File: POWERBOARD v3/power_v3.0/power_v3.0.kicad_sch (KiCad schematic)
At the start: 0 parts

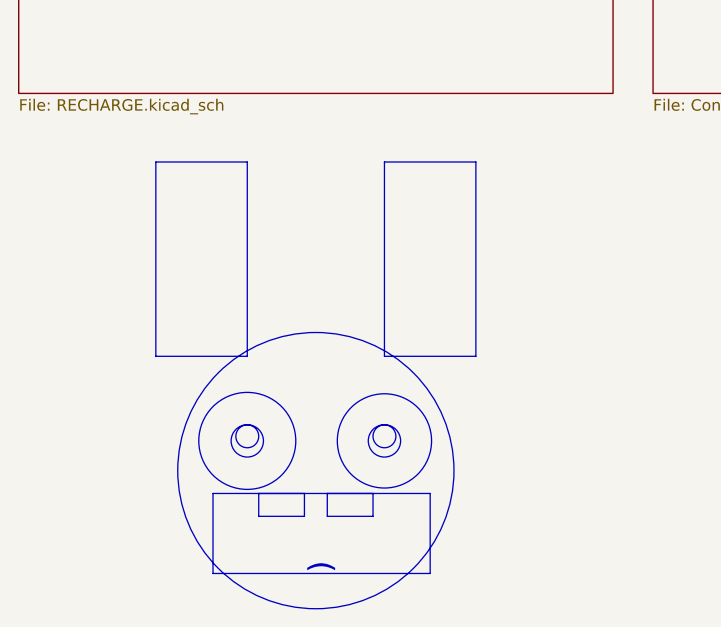
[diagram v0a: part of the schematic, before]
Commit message: added TVS diodes to charging circuit and (almost fully) routed 5.3 to 5V LDO
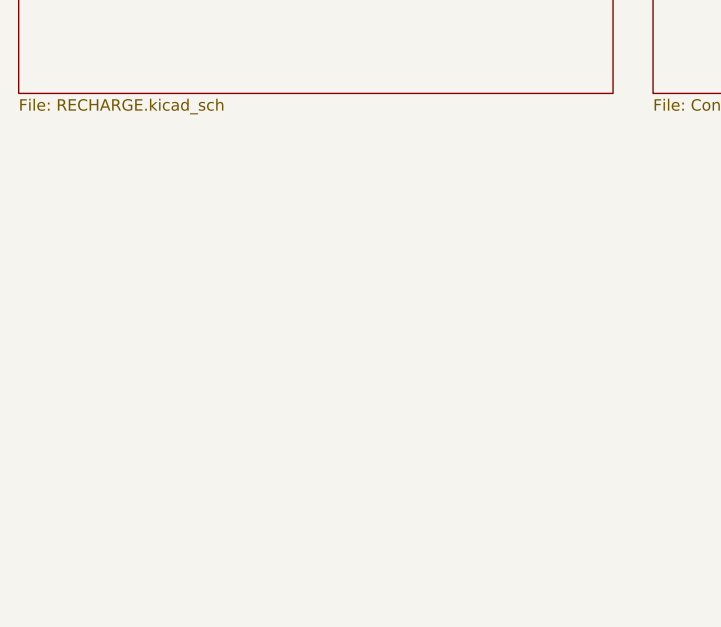
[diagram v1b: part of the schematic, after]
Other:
- note removed: ")"
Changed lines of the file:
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@@
 	(generator_version "10.0")
 	(paper "A4")
-	(rectangle
-		(start 60.96 167.64)
-		(end 85.09 176.53)
-		(stroke
-			(width 0)
-			(type default)
-		)
-		(fill
-			(type none)
-		)
-	)
-	(rectangle
-		(start 80.01 130.81)
-		(end 90.17 152.4)
-		(stroke
-			(width 0)
-			(type default)
-		)
-		(fill
-			(type none)
-		)
-	)
-	(rectangle
-		(start 66.04 167.64)
-		(end 71.12 170.18)
-		(stroke
-			(width 0)
-			(type default)
-		)
-		(fill
-			(type none)
-		)
-	)
-	(circle
-		(center 80.01 161.798)
-		(radius 1.7961)
-		(stroke
-			(width 0)
-			(type solid)
-		)
-		(fill
-			(type none)
-		)
-	)
-	(circle
-		(center 64.77 161.29)
-		(radius 1.27)
-		(stroke
-			(width 0)
-			(type solid)
-		)
-		(fill
-			(type none)
-		)
-	)
-	(circle
-		(center 64.77 161.798)
-		(radius 5.3882)
-		(stroke
-			(width 0)
-			(type default)
-		)
-		(fill
-			(type none)
-		)
-	)
-	(rectangle
-		(start 54.61 130.81)
-		(end 64.77 152.4)
-		(stroke
-			(width 0)
-			(type solid)
-		)
-		(fill
-			(type none)
-		)
-	)
-	(circle
-		(center 80.01 161.29)
-		(radius 1.27)
-		(stroke
-			(width 0)
-			(type default)
-		)
-		(fill
-			(type none)
-		)
-	)
-	(circle
-		(center 72.39 165.1)
-		(radius 15.3455)
-		(stroke
-			(width 0)
-			(type default)
-		)
-		(fill
-			(type none)
-		)
-	)
-	(circle
-		(center 64.77 161.798)
-		(radius 1.7961)
-		(stroke
-			(width 0)
-			(type default)
-		)
-		(fill
-			(type none)
-		)
-	)
-	(circle
-		(center 80.01 161.798)
-		(radius 5.2363)
-		(stroke
-			(width 0)
-			(type default)
-		)
-		(fill
-			(type none)
-		)
-	)
-	(rectangle
-		(start 73.66 167.64)
-		(end 78.74 170.18)
-		(stroke
-			(width 0)
-			(type default)
-		)
-		(fill
-			(type none)
-		)
-	)
-	(text ")\n"
-		(exclude_from_sim no)
-		(at 72.898 176.022 90)
-		(effects
-			(font
-				(size 2.54 2.54)
-			)
-		)
-	)
 	(sheet
 		(at 109.855 63.5)

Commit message: updated file names and added hierarchy schematic, problem with ERC bc of GND
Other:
- removed sheet Conversion 5.3V-5V (page 4)
- removed sheet Conversion battery-5.3V (page 2)
- added sheet Conversion 5.3-5V (5.3to5V.kicad_sch)
- added sheet Conversion battery-5.3V (Conversion battery-5.3V.kicad_sch)
- sheet Charging circuit ports: added SYS; removed none
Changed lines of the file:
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@@
 	(generator_version "10.0")
 	(paper "A4")
+	(text_box "FILE HIERARCHY"
+		(exclude_from_sim no)
+		(at 60.96 88.9 0)
+		(size 157.48 44.45)
+		(margins 0.9525 0.9525 0.9525 0.9525)
+		(stroke
+			(width 0)
+			(type solid)
+		)
+		(fill
+			(type none)
+		)
+		(effects
+			(font
+				(size 1.27 1.27)
+			)
+			(justify left top)
+		)
+	)
+	(wire
+		(pts
+			(xy 153.67 107.95) (xy 175.26 107.95)
+		)
+		(stroke
+			(width 0)
+			(type default)
+		)
+	)
+	(wire
+		(pts
+			(xy 102.87 107.95) (xy 124.46 107.95)
+		)
+		(stroke
+			(width 0)
+			(type default)
+		)
+	)
 	(sheet
-		(at 109.855 63.5)
-		(size 67.31 59.69)
+		(at 124.46 102.87)
+		(size 29.21 19.05)
 		(exclude_from_sim no)
 		(in_bom yes)
@@
 			(color 0 0 0 0)
 		)
-		(property "Sheetname" "Conversion battery-5.3V (page 2)"
-			(at 109.855 62.7884 0)
+		(property "Sheetname" "Conversion battery-5.3V"
+			(at 124.46 102.1584 0)
+			(hide yes)
 			(show_name no)
 			(do_not_autoplace no)
@@
 			)
 		)
-		(property "Sheetfile" "Converison battery-5V.kicad_sch"
-			(at 109.855 123.7746 0)
+		(property "Sheetfile" "Conversion battery-5.3V.kicad_sch"
+			(at 124.46 122.5046 0)
 			(show_name no)
 			(do_not_autoplace no)
@@
 				)
 				(justify left top)
+			)
+		)
+		(pin "SYS" input
+			(at 124.46 107.95 180)
+			(effects
+				(font
+					(size 1.27 1.27)
+				)
+				(justify left)
+			)
+		)
+		(pin "output_at_5.3" output
+			(at 153.67 107.95 0)
+			(effects
+				(font
+					(size 1.27 1.27)
+				)
+				(justify right)
 			)
 		)
@@
 	)
 	(sheet
-		(at 181.61 63.5)
-		(size 66.675 59.69)
+		(at 73.66 102.87)
+		(size 29.21 19.05)
 		(exclude_from_sim no)
 		(in_bom yes)
@@
 			(color 0 0 0 0)
 		)
-		(property "Sheetname" "Conversion 5.3V-5V (page 4)"
-			(at 181.61 62.7884 0)
+		(property "Sheetname" "Charging circuit"
+			(at 73.66 102.1584 0)
 			(show_name no)
 			(do_not_autoplace no)
@@
 			)
 		)
-		(property "Sheetfile" "5to3.3V.kicad_sch"
-			(at 181.61 123.7746 0)
+		(property "Sheetfile" "RECHARGE.kicad_sch"
+			(at 73.66 122.5046 0)
 			(show_name no)
 			(do_not_autoplace no)
@@
 				)
 				(justify left top)
+			)
+		)
+		(pin "SYS" output
+			(at 102.87 107.95 0)
+			(effects
+				(font
+					(size 1.27 1.27)
+				)
+				(justify right)
+			)
+		)
+		(instances
+			(project "power_v3.0"
+				(path "/432bcdcf-747a-4fa0-b87b-096f44260199"
+					(page "3")
+				)
+			)
+		)
+	)
+	(sheet
+		(at 175.26 102.87)
+		(size 29.21 19.05)
+		(exclude_from_sim no)
+		(in_bom yes)
+		(on_board yes)
+		(dnp no)
+		(fields_autoplaced yes)
+		(stroke
+			(width 0.1524)
+			(type solid)
+		)
+		(fill
+			(color 0 0 0 0)
+		)
+		(property "Sheetname" "Conversion 5.3-5V"
+			(at 175.26 102.1584 0)
+			(show_name no)
+			(do_not_autoplace no)
+			(effects
+				(font
+					(size 1.27 1.27)
+				)
+				(justify left bottom)
+			)
+		)
+		(property "Sheetfile" "5.3to5V.kicad_sch"
+			(at 175.26 122.5046 0)
+			(show_name no)
+			(do_not_autoplace no)
+			(effects
+				(font
+					(size 1.27 1.27)
+				)
+				(justify left top)
+			)
+		)
+		(pin "input_at_5.3" input
+			(at 175.26 107.95 180)
+			(effects
+				(font
+					(size 1.27 1.27)
+				)
+				(justify left)
 			)
 		)
@@
 				)
 			)
-		)
-	)
-	(sheet
-		(at 39.37 63.5)
-		(size 66.04 59.69)
-		(exclude_from_sim no)
-		(in_bom yes)
-		(on_board yes)
-		(dnp no)
-		(fields_autoplaced yes)
-		(stroke
-			(width 0.1524)
-			(type solid)
-		)
-		(fill
-			(color 0 0 0 0)
-		)
-		(property "Sheetname" "Charging circuit"
-			(at 39.37 62.7884 0)
-			(show_name no)
-			(do_not_autoplace no)
-			(effects
-				(font
-					(size 1.27 1.27)
-				)
-				(justify left bottom)
-			)
-		)
-		(property "Sheetfile" "RECHARGE.kicad_sch"
-			(at 39.37 123.7746 0)
-			(show_name no)
-			(do_not_autoplace no)
-			(effects
-				(font
-					(size 1.27 1.27)
-				)
-				(justify left top)
-			)
-		)
-		(instances
-			(project "power_v3.0"
-				(path "/432bcdcf-747a-4fa0-b87b-096f44260199"
-					(page "3")
-				)
-			)
